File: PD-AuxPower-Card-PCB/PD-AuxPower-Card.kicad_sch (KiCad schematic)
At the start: 52 parts, among them J1 1.27mm 1x4P, J2 1.27mm 1x4P, J3 USB_C_Receptacle_USB2.0, SW1 TSA017A2510A, SW2 K3-1296S-E1, SW3 K3-1296S-E1, U12 STM32L432KCUx, U2 FUSB302BMPX, U3 TPS62177DQC, U4 K24C02

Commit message: Initial commit. Add source file of PCB and Firmware, the firmware not support any communication yet, but only can show LED effect for its alive.
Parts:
- removed R1: 160k, Resistor_SMD:R_0603_1608Metric, symbol Device:R_Small
- removed R6: 51k, Resistor_SMD:R_0603_1608Metric, symbol Device:R_Small
- R25, R26, R27, R28: value 499 -> 2k
- R5: value 1k -> 2k
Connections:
- net +3V3: no longer U3.3 (EN)
- net GND: now also U3.5 (FB)
- net I2C1_SCL: now also U4.1 (SCL); no longer U4.3 (SDA)
- net I2C1_SDA: now also U4.3 (SDA); no longer U4.1 (SCL)
- net VBUS: now also U3.3 (EN)
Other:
- moved on the sheet: C2, C3, TP1

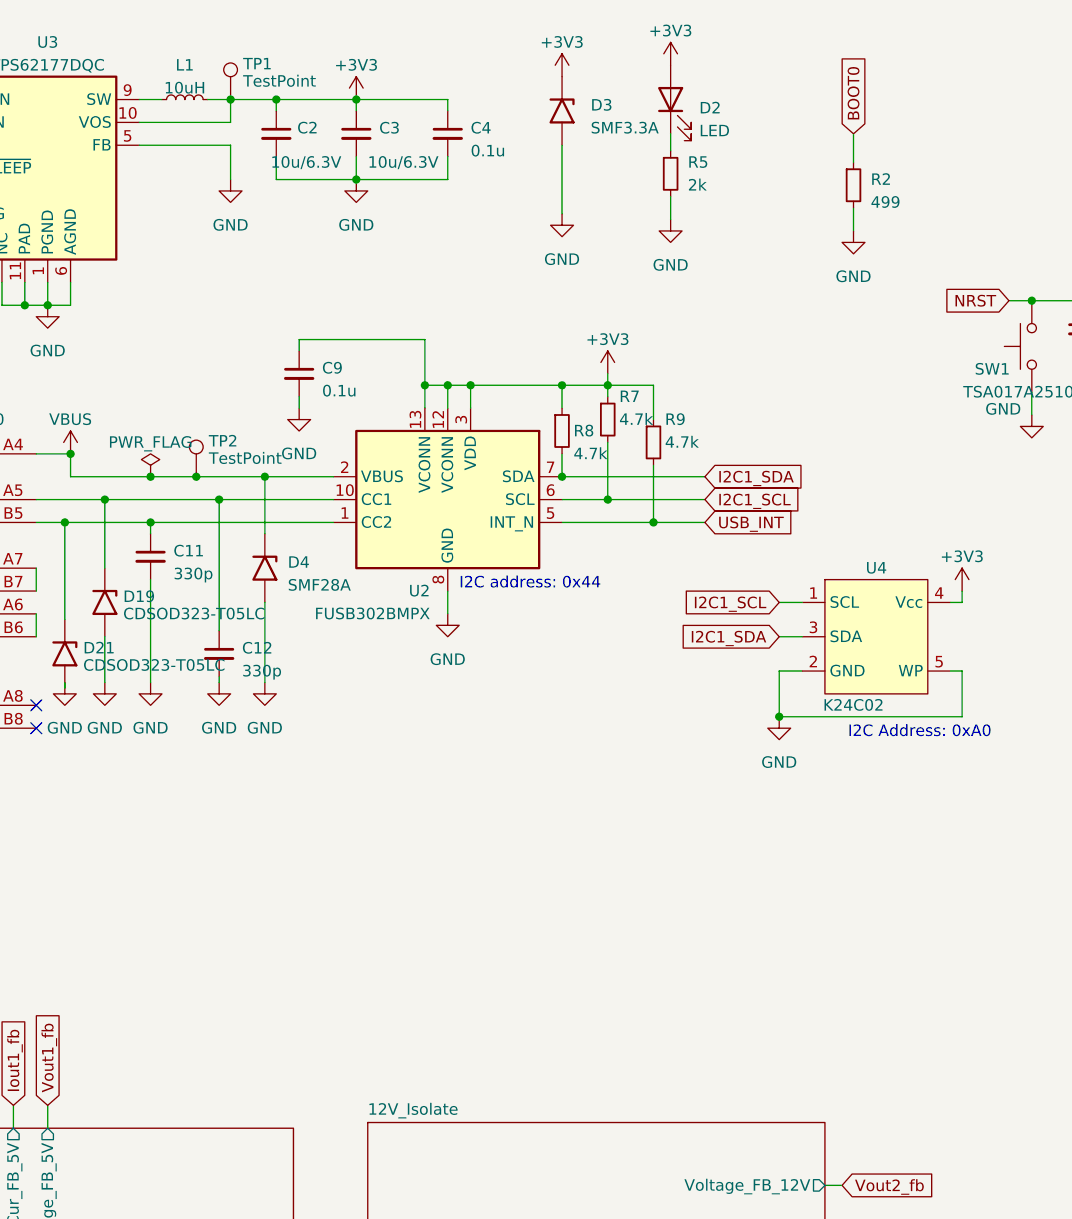
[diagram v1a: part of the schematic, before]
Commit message: FEAT: Add house keeping timer (tim16 )for checking switches status. Add I2C test function asking FUSB302B some data.
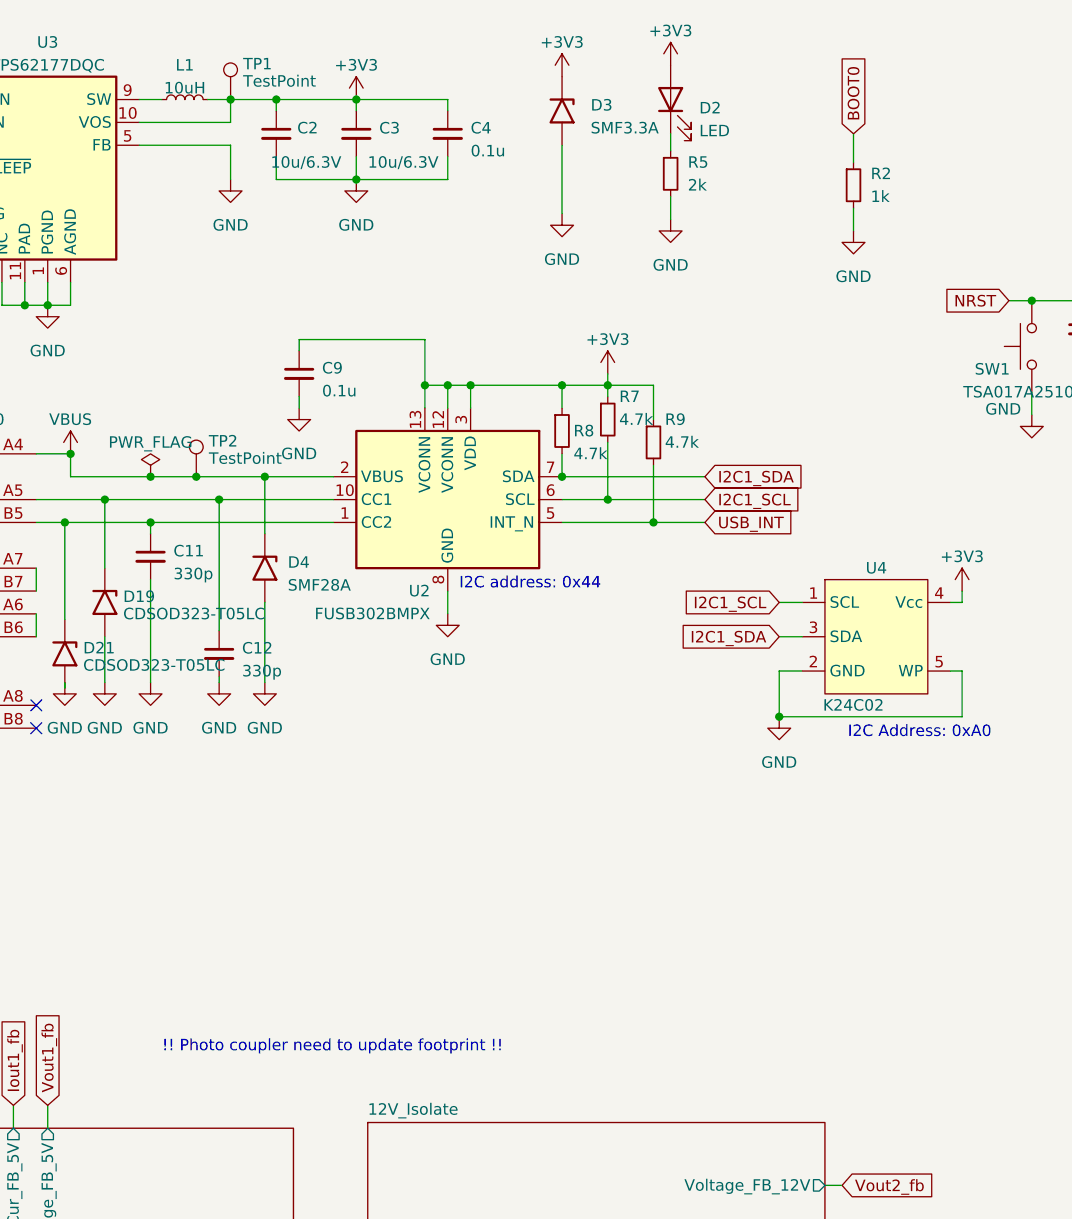
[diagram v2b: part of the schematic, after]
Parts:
- R2: value 499 -> 1k
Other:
- note added: "!! Photo coupler need to update footprint !!"
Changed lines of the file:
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@@
+    (effects (font (size 1.27 1.27)) (justify left bottom))
+  )
+  (text "!! Photo coupler need to update footprint !!" (at 64.77 132.715 0)
     (effects (font (size 1.27 1.27)) (justify left bottom))
   )
@@
   (symbol (lib_id "Device:R_Small") (at 141.605 36.195 0) (unit 1)
     (in_bom yes) (on_board yes) (dnp no) (fields_autoplaced)
-    (property "Reference" "R2" (at 143.51 35.56 0)
-      (effects (font (size 1.27 1.27)) (justify left))
-    )
-    (property "Value" "499" (at 143.51 38.1 0)
-      (effects (font (size 1.27 1.27)) (justify left))
-    )
+    (property "Reference" "R2" (at 143.51 34.925 0)
+      (effects (font (size 1.27 1.27)) (justify left))
+    )
+    (property "Value" "1k" (at 143.51 37.465 0)
+      (effects (font (size 1.27 1.27)) (justify left))
+    )

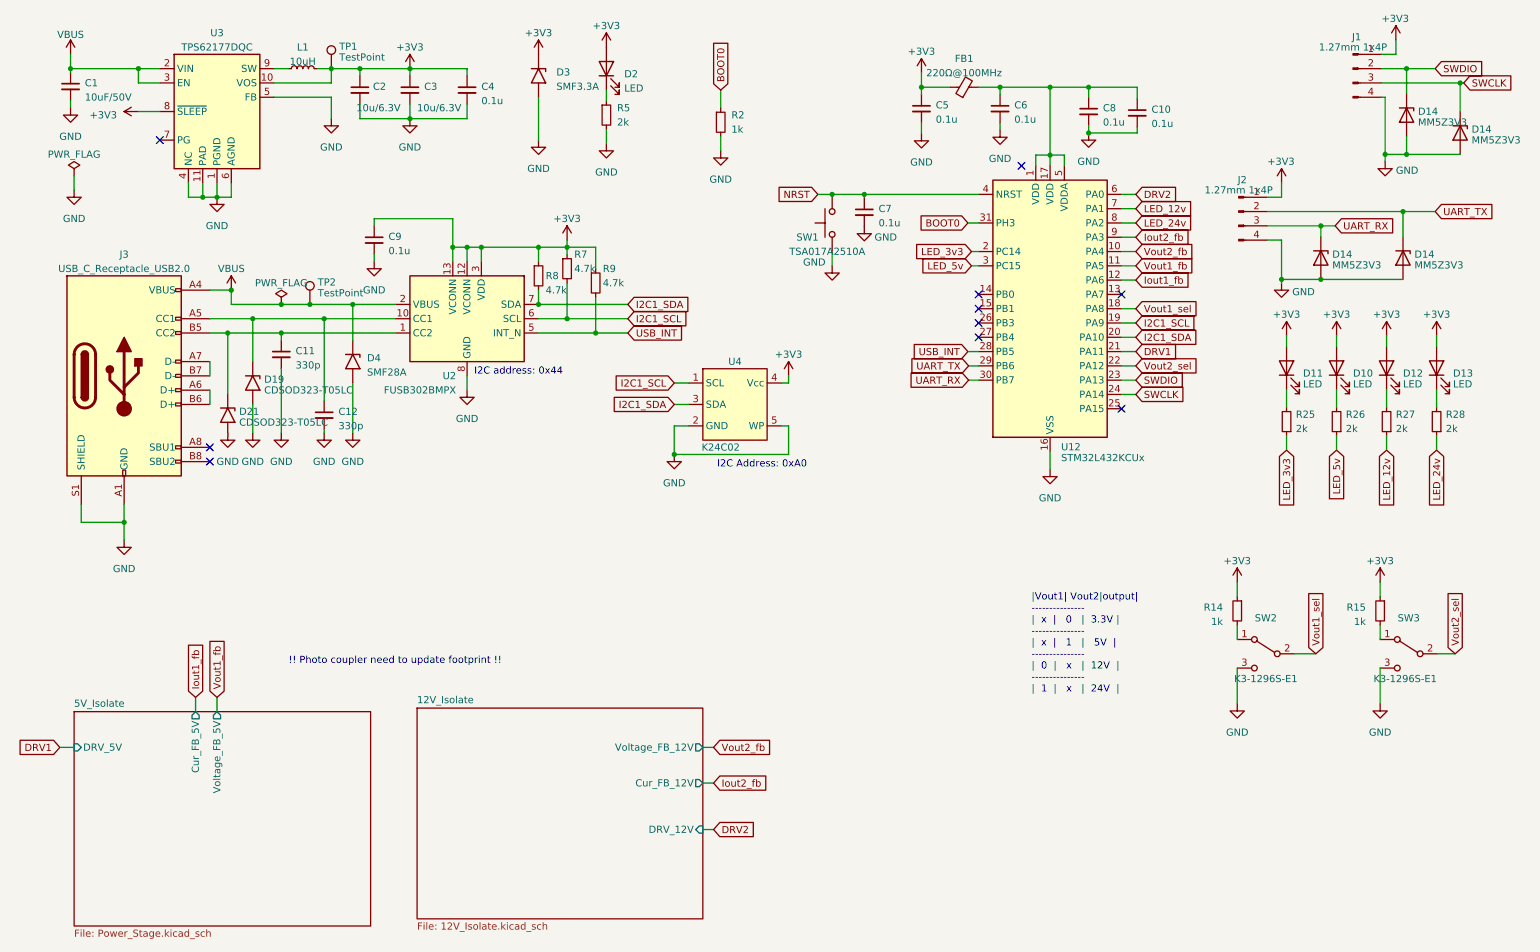
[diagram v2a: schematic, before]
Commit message: FEAT: Revolution PCB to ver 1.0. Change COMP1+ to 3v3 current sense, COMP2+ to 12V current sense and 12V LED to GPIO7 output. Modify PCB layout.
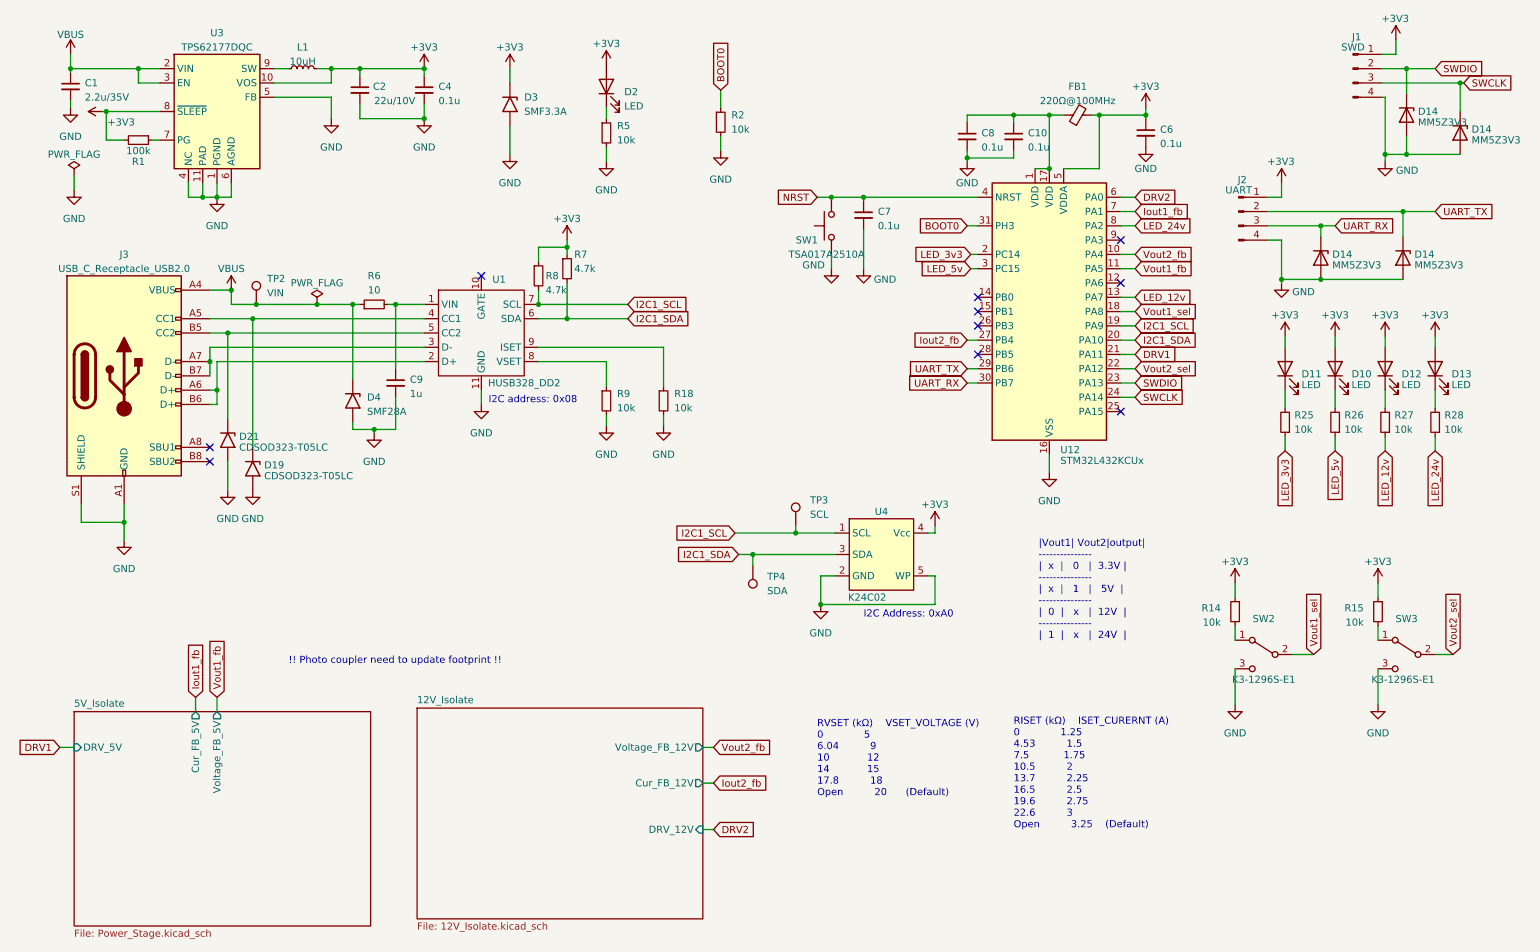
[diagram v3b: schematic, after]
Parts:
- removed C11, C12: 330p, Capacitor_SMD:C_0402_1005Metric, symbol Device:C_Small
- removed C3: 10u/6.3V, Capacitor_SMD:C_0603_1608Metric, symbol Device:C_Small
- removed C5: 0.1u, Capacitor_SMD:C_0402_1005Metric, symbol Device:C_Small
- removed TP1: TestPoint, TestPoint:TestPoint_Pad_D1.0mm, symbol Connector:TestPoint
- removed U2: FUSB302BMPX, Package_DFN_QFN:WQFN-14-1EP_2.5x2.5mm_P0.5mm_EP1.45x1.45mm, symbol Interface_USB:FUSB302BMPX
- added R1: 100k, Resistor_SMD:R_0603_1608Metric, symbol Device:R_Small
- added R18: 10k, Resistor_SMD:R_0603_1608Metric, symbol Device:R_Small
- added R6: 10, Resistor_SMD:R_0603_1608Metric, symbol Device:R_Small
- added TP3: SCL, TestPoint:TestPoint_Pad_D1.0mm, symbol Connector:TestPoint
- added TP4: SDA, TestPoint:TestPoint_Pad_D1.0mm, symbol Connector:TestPoint
- added U1: HUSB328_DD2, Package_DFN_QFN:DFN-10-1EP_3x3mm_P0.5mm_EP1.65x2.38mm, symbol Johnson_lib:HUSB238002_DD
- C1: value 10uF/50V -> 2.2u/35V
- C2: value 10u/6.3V -> 22u/10V; footprint Capacitor_SMD:C_0603_1608Metric -> Capacitor_SMD:C_1206_3216Metric
- C9: value 0.1u -> 1u; footprint Capacitor_SMD:C_0402_1005Metric -> Capacitor_SMD:C_0603_1608Metric
- J1: value 1.27mm 1x4P -> SWD
- J2: value 1.27mm 1x4P -> UART
- R14, R15: value 1k -> 10k
- R2: value 1k -> 10k; footprint Resistor_SMD:R_0603_1608Metric -> Resistor_SMD:R_0402_1005Metric
- R25, R26, R27, R28, R5: value 2k -> 10k
- R9: value 4.7k -> 10k; footprint Resistor_SMD:R_0402_1005Metric -> Resistor_SMD:R_0603_1608Metric
- TP2: value TestPoint -> VIN
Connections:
- net +3V3: now also C6.1, FB1.2, U12.5 (VDDA), R1.2; no longer C9.1, FB1.1, R9.1
- net GND: now also R9.2, R18.2, U1.11 (GND)
- net I2C1_SCL: now also R8.2, TP3.1, U1.7 (SCL); no longer R7.2
- net I2C1_SDA: now also R7.2, TP4.1, U1.6 (SDA); no longer R8.2
- net Iout1_fb: now also U12.7 (PA1); no longer U12.12 (PA6)
- net Iout2_fb: now also U12.27 (PB4); no longer U12.9 (PA3)
- net LED_12v: now also U12.13 (PA7); no longer U12.7 (PA1)
- net VBUS: now also R6.1
- net at C10.1, C8.1, U12.1 (VDD)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: now also FB1.1; no longer C6.1, FB1.2, U12.5 (VDDA)
- net at D21.1 (A1), J3.B5 (CC2): now also U1.5 (CC2)
- net at D19.1 (A1), J3.A5 (CC1): now also U1.4 (CC1)
- net at U3.7 (PG): now also R1.1
- net at J3.A6 (D+), J3.B6 (D+): now also U1.2 (D+)
- net at J3.A7 (D-), J3.B7 (D-): now also U1.3 (D-)
- net USB_INT: no longer names the net of U12.28 (PB5)
- net USB_INT: no longer R9.2
- new net: R9.1, U1.8 (VSET)
- new net: C9.1, R6.2, U1.1 (VIN)
- new net: R18.1, U1.9 (ISET)
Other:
- note added: "I2C address: 0x08"
- note added: "RISET (kΩ) ISET_CURERNT (A) 0 1.25 4.53 1.5 7.5 1.75 10.5 2 13.7 2.25 16.5 2.5 19.6 2.75 22.6 3 Open 3.25 (Default)"
- note added: "RVSET (kΩ) VSET_VOLTAGE (V) 0 5 6.04 9 10 12 14 15 17.8 18 Open 20 (Default)"
- note removed: "I2C address: 0x44"
- company: (none) -> Habonroof Playground
- title: (none) -> Tiny-Aux card power supply Main board
- moved on the sheet: C10, C4, C6, C7, C8, C9, D19, D2, D21, D4, FB1, R5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

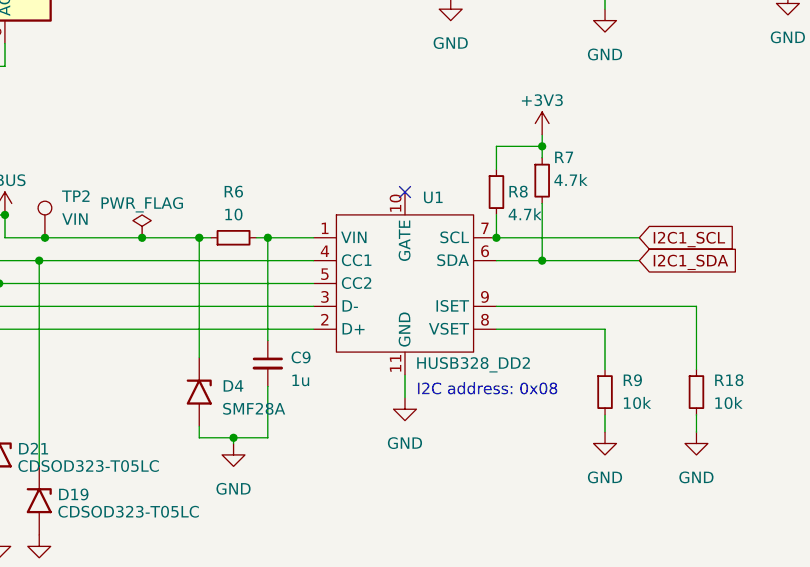
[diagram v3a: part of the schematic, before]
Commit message: HW: FEAT: Relayout circuit and some adjustment. FW: Change .ico file to match schematic, add COMP for current limiting
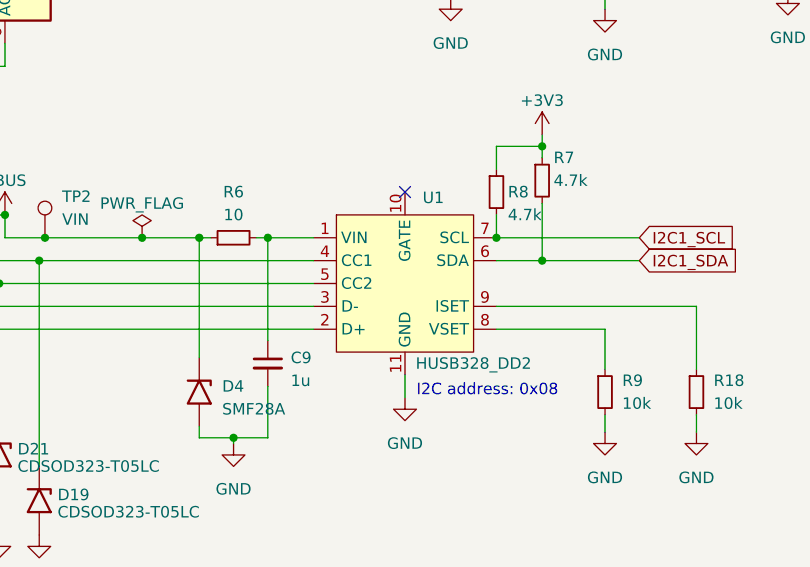
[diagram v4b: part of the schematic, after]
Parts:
- U1: symbol Johnson_lib:HUSB238002_DD -> Johnson's:HUSB238002_DD
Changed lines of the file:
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@@
     )
   )
-  (symbol (lib_id "Johnson_lib:HUSB238002_DD") (at 99.06 76.2 0) (unit 1)
+  (symbol (lib_id "Johnson's:HUSB238002_DD") (at 99.06 76.2 0) (unit 1)
     (in_bom yes) (on_board yes) (dnp no)
     (property "Reference" "U1" (at 101.0159 64.135 0)

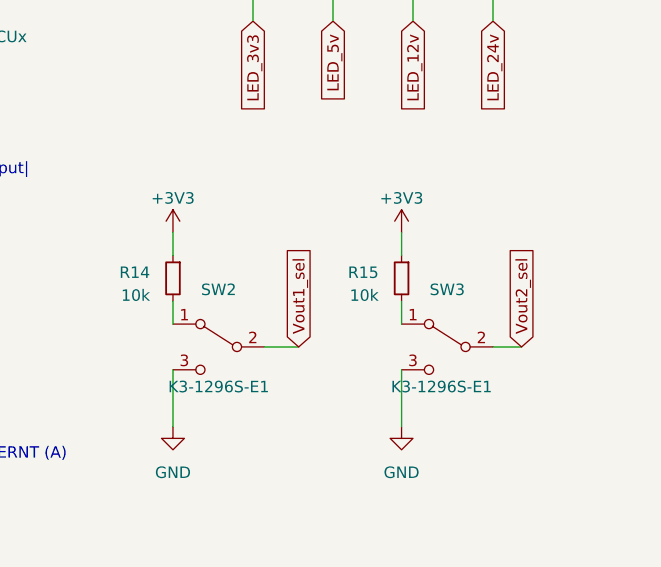
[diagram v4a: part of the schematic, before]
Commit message: FEAT: Add Matlab file (Octave capable) for calculation transformer parameter. Modify PCB schematic Redefine pinout, ISR and peripherial
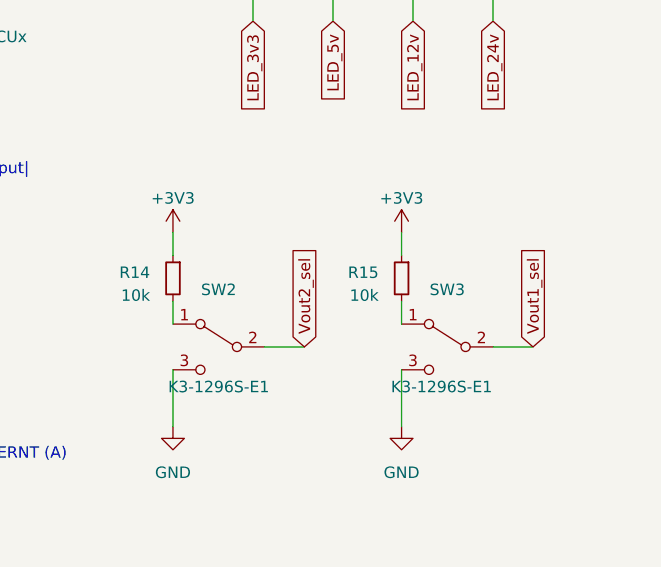
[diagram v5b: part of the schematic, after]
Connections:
- net Vout1_sel: now also SW3.2 (B); no longer SW2.2 (B)
- net Vout2_sel: now also SW2.2 (B); no longer SW3.2 (B)
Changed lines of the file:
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@@
+    (stroke (width 0) (type default))
+  )
+  (wire (pts (xy 243.205 130.81) (xy 247.65 130.81))
     (stroke (width 0) (type default))
   )
@@
     (stroke (width 0) (type default))
   )
+  (wire (pts (xy 268.605 130.81) (xy 273.05 130.81))
+    (stroke (width 0) (type default))
+  )
   (wire (pts (xy 77.47 35.56) (xy 88.9 35.56))
     (stroke (width 0) (type default))
@@
     (stroke (width 0) (type default))
   )
-  (wire (pts (xy 243.205 130.81) (xy 247.015 130.81))
-    (stroke (width 0) (type default))
-  )
   (wire (pts (xy 69.85 68.58) (xy 76.2 68.58))
     (stroke (width 0) (type default))
@@
   )
   (wire (pts (xy 185.42 54.61) (xy 187.325 54.61))
-    (stroke (width 0) (type default))
-  )
-  (wire (pts (xy 268.605 130.81) (xy 271.78 130.81))
     (stroke (width 0) (type default))
   )
@@
     )
   )
-  (global_label "Vout1_sel" (shape input) (at 247.015 130.81 90) (fields_autoplaced)
-    (effects (font (size 1.27 1.27)) (justify left))
-    (property "Intersheetrefs" "${INTERSHEET_REFS}" (at 247.015 118.8329 90)
+  (global_label "Vout1_sel" (shape input) (at 273.05 130.81 90) (fields_autoplaced)
+    (effects (font (size 1.27 1.27)) (justify left))
+    (property "Intersheetrefs" "${INTERSHEET_REFS}" (at 273.05 118.8329 90)
       (effects (font (size 1.27 1.27)) (justify left) hide)
     )
@@
     )
   )
-  (global_label "Vout2_sel" (shape input) (at 271.78 130.81 90) (fields_autoplaced)
-    (effects (font (size 1.27 1.27)) (justify left))
-    (property "Intersheetrefs" "${INTERSHEET_REFS}" (at 271.78 118.8329 90)
-      (effects (font (size 1.27 1.27)) (justify left) hide)
-    )
+  (global_label "Vout2_sel" (shape input) (at 247.65 130.81 90) (fields_autoplaced)
+    (effects (font (size 1.27 1.27)) (justify left))
+    (property "Intersheetrefs" "${INTERSHEET_REFS}" (at 247.65 118.8329 90)
+      (effects (font (size 1.27 1.27)) (justify left) hide)
+    )
